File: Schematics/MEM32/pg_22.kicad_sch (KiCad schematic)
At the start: 2 parts, among them U1806 XLRULOGIC, U1903 TSXXPAL

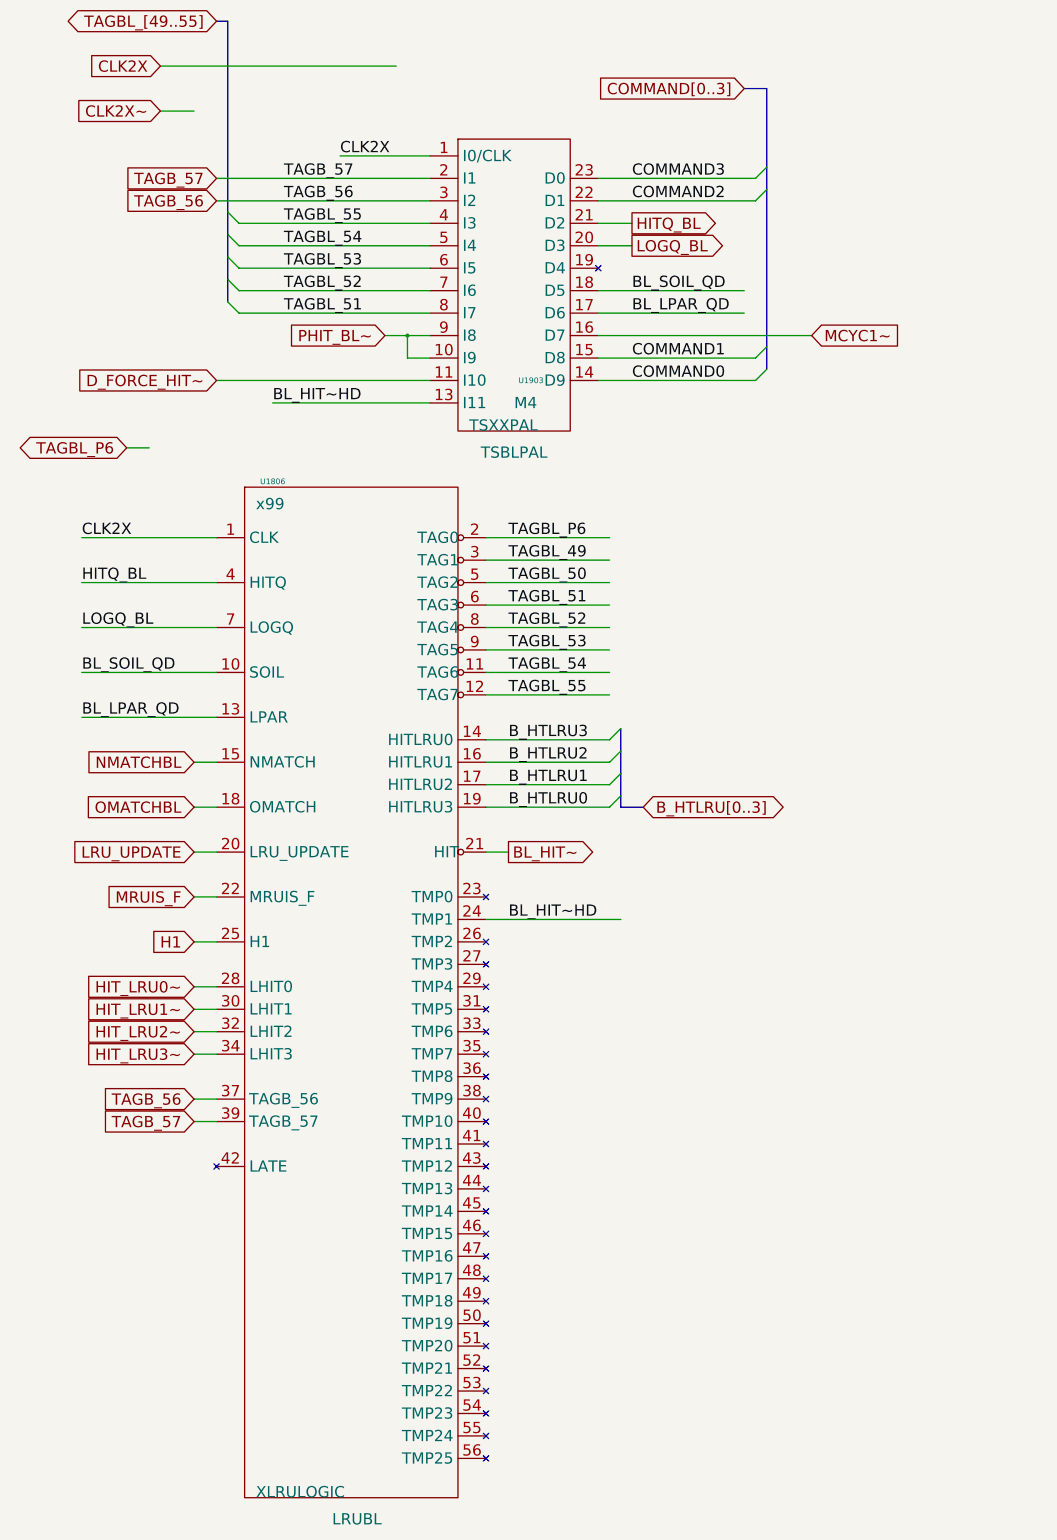
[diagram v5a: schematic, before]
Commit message: MEM32: Move LPAR from TSXXPAL to XLRULOGIC
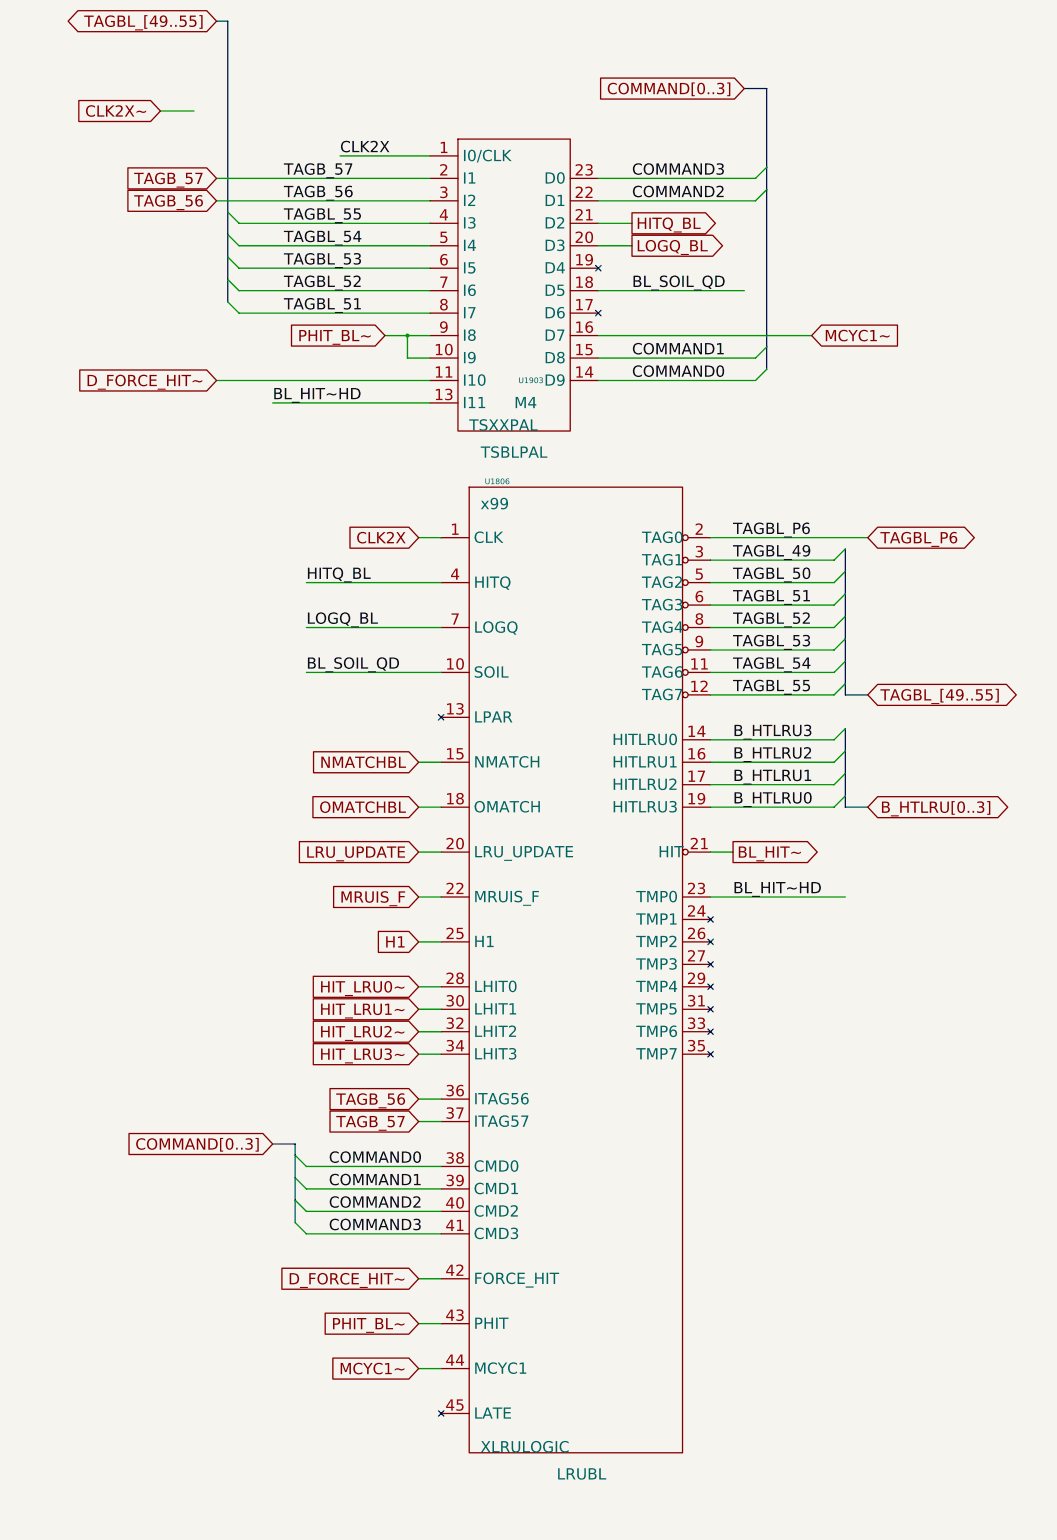
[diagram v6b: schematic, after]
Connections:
- net BL_HIT~HD: now also U1806.23 (TMP0); no longer U1806.24 (TMP1)
- net COMMAND0: now also U1806.38 (CMD0)
- net COMMAND1: now also U1806.39 (CMD1)
- net COMMAND2: now also U1806.40 (CMD2)
- net COMMAND3: now also U1806.41 (CMD3)
- net D_FORCE_HIT~: now also U1806.42 (FORCE_HIT)
- net MCYC1~: now also U1806.44 (MCYC1)
- net PHIT_BL~: now also U1806.43 (PHIT)
- net TAGB_56: now also U1806.36 (ITAG56); no longer U1806.37 (TAGB_56)
- net TAGB_57: now also U1806.37 (ITAG57); no longer U1806.39 (TAGB_57)
- net BL_LPAR_QD: no longer names the net of U1903.17 (D6)
- net BL_LPAR_QD: no longer U1806.13 (LPAR)
- no-connect marks 27 -> 11

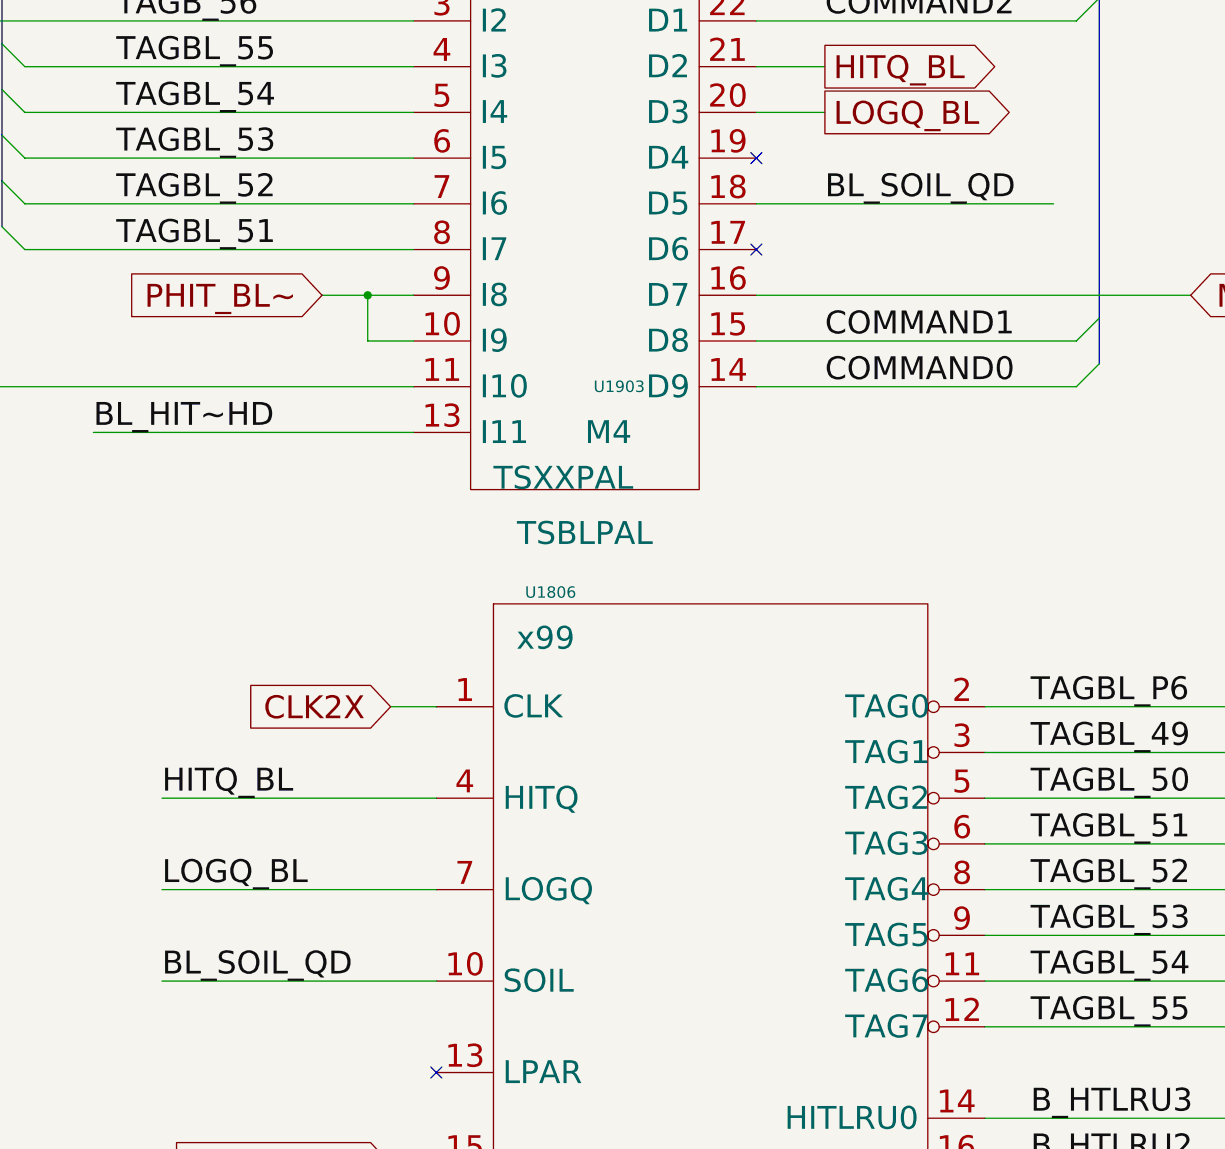
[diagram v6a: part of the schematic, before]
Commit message: MEM32: Move soil_qd from TSXXPAL to XLRULOGIC, tested to 15.5s(rm129)
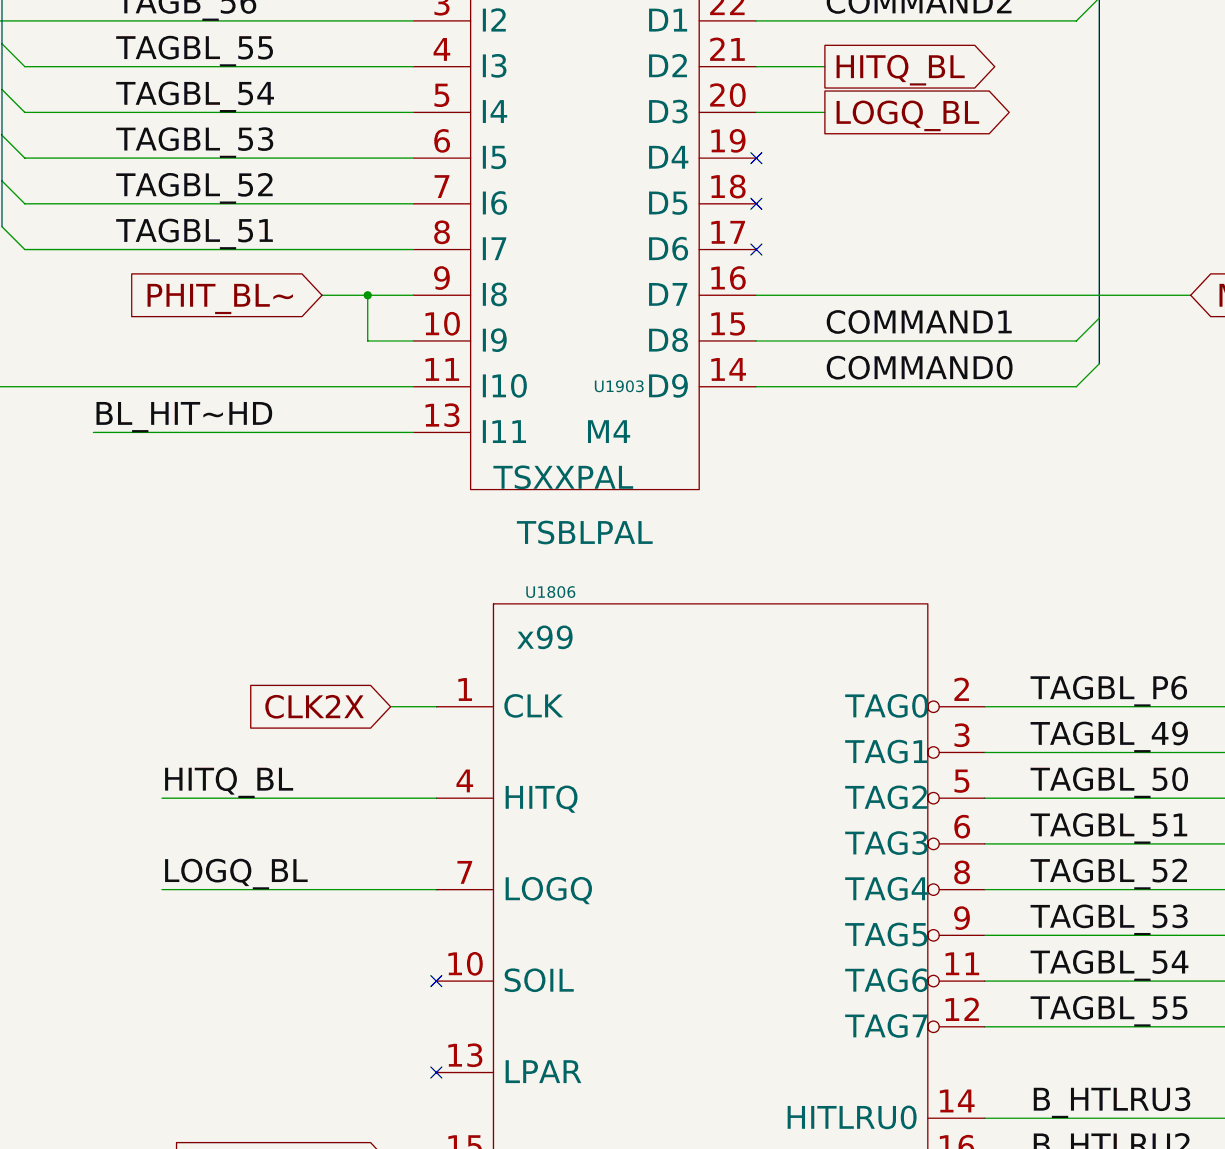
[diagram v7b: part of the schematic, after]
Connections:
- net BL_SOIL_QD: no longer names the net of U1903.18 (D5)
- net BL_SOIL_QD: no longer U1806.10 (SOIL)
- no-connect marks 11 -> 13
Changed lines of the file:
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@@
   (no_connect (at 116.84 172.72))
   (no_connect (at 177.8 223.52))
+  (no_connect (at 152.4 76.2))
+  (no_connect (at 116.84 162.56))
   (no_connect (at 177.8 238.76))
   (no_connect (at 177.8 243.84))
@@
     (stroke (width 0) (type default))
   )
-  (wire (pts (xy 86.36 162.56) (xy 116.84 162.56))
-    (stroke (width 0) (type default))
-  )
   (wire (pts (xy 152.4 55.88) (xy 187.96 55.88))
     (stroke (width 0) (type default))
@@
     (stroke (width 0) (type default))
   )
-  (wire (pts (xy 185.42 76.2) (xy 152.4 76.2))
-    (stroke (width 0) (type default))
-  )
   (wire (pts (xy 53.34 35.56) (xy 60.96 35.56))
     (stroke (width 0) (type default))
@@
     (effects (font (size 2.54 2.54)) (justify left bottom))
   )
-  (label "BL_SOIL_QD" (at 86.36 162.56 0) (fields_autoplaced)
-    (effects (font (size 2.54 2.54)) (justify left bottom))
-  )
   (label "TAGBL_54" (at 182.88 162.56 0) (fields_autoplaced)
     (effects (font (size 2.54 2.54)) (justify left bottom))
@@
     (effects (font (size 2.54 2.54)) (justify left bottom))
   )
-  (label "BL_SOIL_QD" (at 160.02 76.2 0) (fields_autoplaced)
-    (effects (font (size 2.54 2.54)) (justify left bottom))
-  )

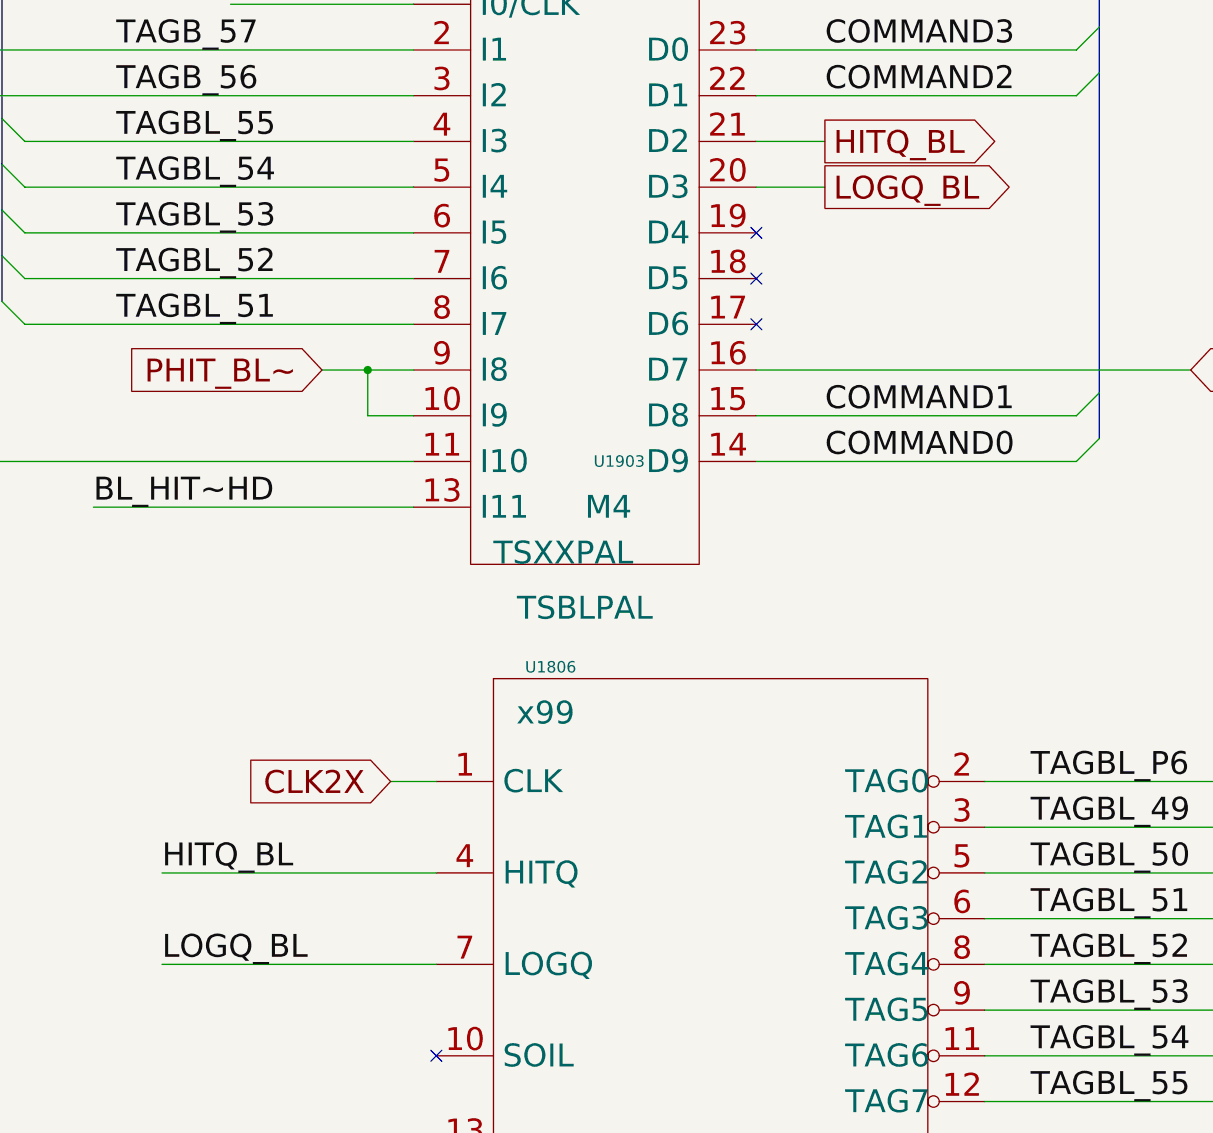
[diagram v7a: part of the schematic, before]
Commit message: MEM32: Mov LOGQ to XLRULOGIC, tested to 4.3s (rm130)
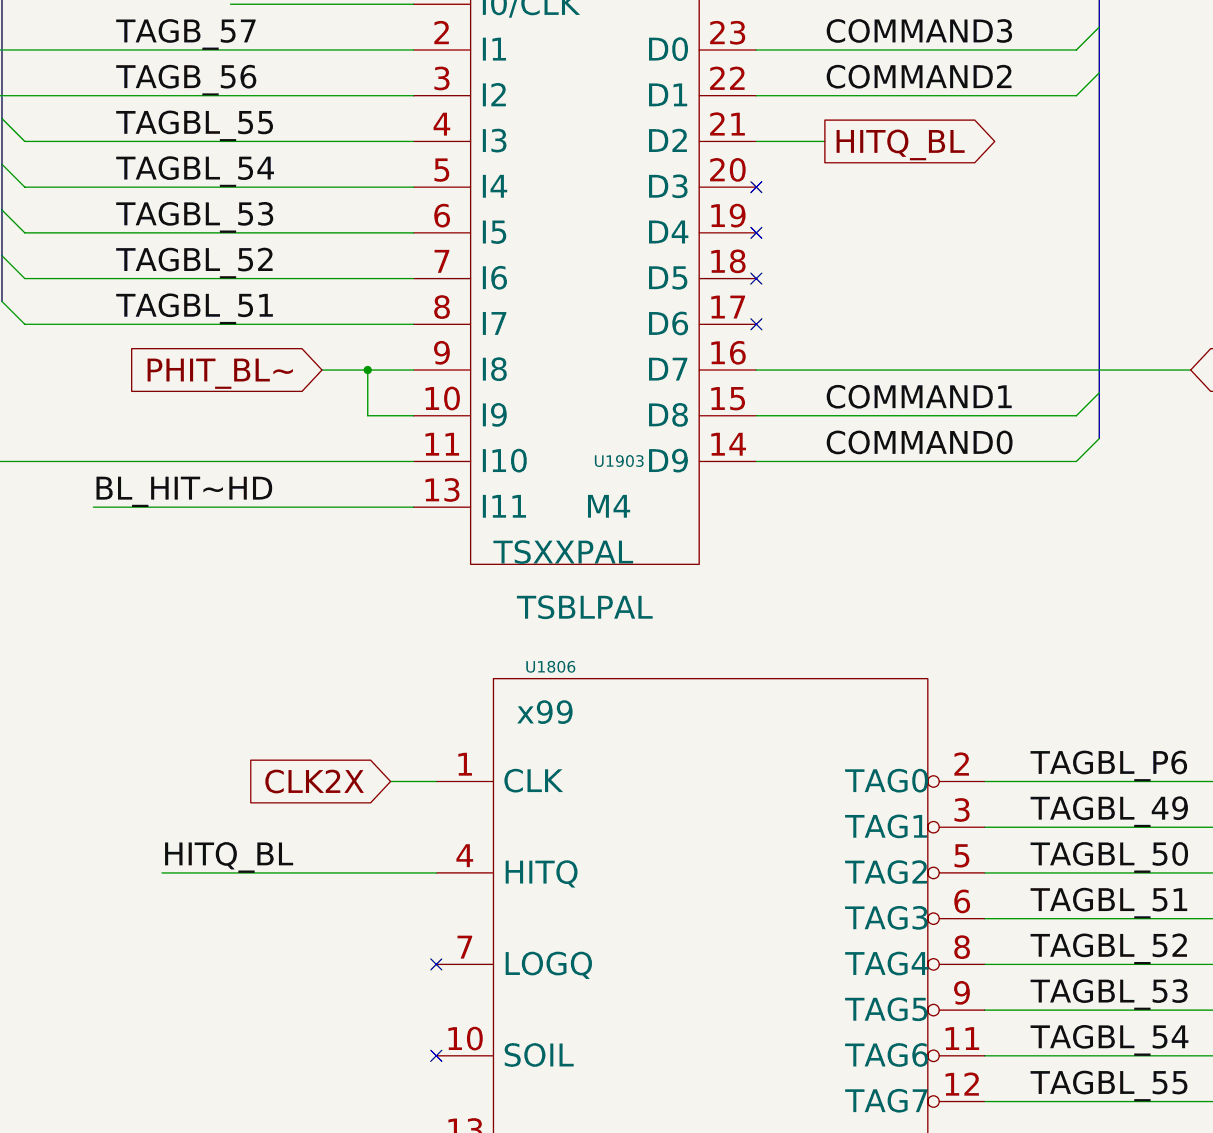
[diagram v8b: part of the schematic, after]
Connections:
- net LOGQ_BL: no longer names the net of U1903.20 (D3)
- net LOGQ_BL: no longer U1806.7 (LOGQ)
- no-connect marks 13 -> 15
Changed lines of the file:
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@@
   (no_connect (at 152.4 71.12))
   (no_connect (at 116.84 330.2))
+  (no_connect (at 116.84 152.4))
   (no_connect (at 177.8 228.6))
-  (no_connect (at 177.8 218.44))
   (no_connect (at 177.8 233.68))
   (no_connect (at 177.8 248.92))
   (no_connect (at 152.4 81.28))
+  (no_connect (at 177.8 218.44))
   (no_connect (at 116.84 172.72))
   (no_connect (at 177.8 223.52))
@@
   (no_connect (at 177.8 238.76))
   (no_connect (at 177.8 243.84))
+  (no_connect (at 152.4 66.04))
   (bus_entry (at 83.82 276.86) (size 2.54 2.54)
     (stroke (width 0) (type default))
@@
     (stroke (width 0) (type default))
   )
-  (wire (pts (xy 152.4 66.04) (xy 160.02 66.04))
-    (stroke (width 0) (type default))
-  )
   (wire (pts (xy 111.76 213.36) (xy 116.84 213.36))
     (stroke (width 0) (type default))
@@
     (stroke (width 0) (type default))
   )
-  (wire (pts (xy 86.36 152.4) (xy 116.84 152.4))
-    (stroke (width 0) (type default))
-  )
   (wire (pts (xy 177.8 152.4) (xy 205.74 152.4))
     (stroke (width 0) (type default))
@@
   )
   (label "TAGBL_52" (at 182.88 152.4 0) (fields_autoplaced)
-    (effects (font (size 2.54 2.54)) (justify left bottom))
-  )
-  (label "LOGQ_BL" (at 86.36 152.4 0) (fields_autoplaced)
     (effects (font (size 2.54 2.54)) (justify left bottom))
   )
@@
     )
   )
-  (global_label "LOGQ_BL" (shape output) (at 160.02 66.04 0) (fields_autoplaced)
-    (effects (font (size 2.54 2.54)) (justify left))
-    (property "Intersheet References" "${INTERSHEET_REFS}" (at 181.2955 65.8813 0)
-      (effects (font (size 1.905 1.905)) (justify left))
-    )
-  )
